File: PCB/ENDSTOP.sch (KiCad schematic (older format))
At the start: 4 parts, among them J9 ENDSTOP_CONN, SW3 ENDSTOP

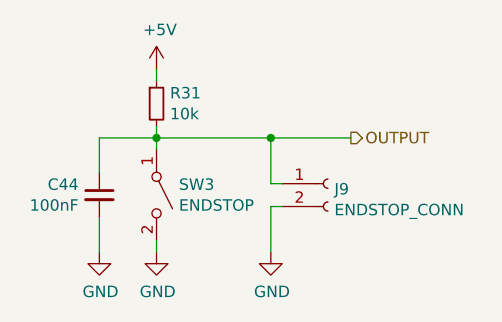
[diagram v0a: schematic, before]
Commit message: Added remaining test points
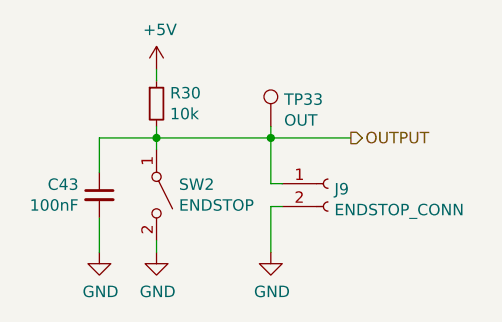
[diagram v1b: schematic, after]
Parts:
- added TP33: OUT, symbol Connector:TestPoint
- renumbered C44 to C43, R31 to R30, SW3 to SW2
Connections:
- net OUTPUT: now also TP33.1
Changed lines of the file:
@@
 OUTPUT
 $Comp
-L Switch:SW_SPST SW3
+L Switch:SW_SPST SW2
 U 1 1 5E8A8DC4
 P 6150 4150
-F 0 "SW3" V 6104 4248 50  0000 L CNN
+F 0 "SW2" V 6104 4248 50  0000 L CNN
 F 1 "ENDSTOP" V 6195 4248 50  0000 L CNN
 F 2 "" H 6150 4150 50  0001 C CNN
@@
 $EndComp
 $Comp
-L Device:C_Small C44
+L Device:C_Small C43
 U 1 1 5E8A9073
 P 5900 4150
-F 0 "C44" H 5809 4196 50  0000 R CNN
+F 0 "C43" H 5809 4196 50  0000 R CNN
 F 1 "100nF" H 5809 4105 50  0000 R CNN
 F 2 "" H 5900 4150 50  0001 C CNN
@@
 $EndComp
 $Comp
-L Device:R_Small R31
+L Device:R_Small R30
 U 1 1 5E8A974E
 P 6150 3750
-F 0 "R31" H 6209 3796 50  0000 L CNN
+F 0 "R30" H 6209 3796 50  0000 L CNN
 F 1 "10k" H 6209 3705 50  0000 L CNN
 F 2 "" H 6150 3750 50  0001 C CNN
@@
 	6150 3900 6150 3950
 $Comp
-L power:GND #PWR0125
+L power:GND #PWR0122
 U 1 1 5E8A9B1B
 P 5900 4400
-F 0 "#PWR0125" H 5900 4150 50  0001 C CNN
+F 0 "#PWR0122" H 5900 4150 50  0001 C CNN
 F 1 "GND" H 5905 4227 50  0000 C CNN
 F 2 "" H 5900 4400 50  0001 C CNN
@@
 $EndComp
 $Comp
-L power:GND #PWR0127
+L power:GND #PWR0124
 U 1 1 5E8A9B96
 P 6150 4400
-F 0 "#PWR0127" H 6150 4150 50  0001 C CNN
+F 0 "#PWR0124" H 6150 4150 50  0001 C CNN
 F 1 "GND" H 6155 4227 50  0000 C CNN
 F 2 "" H 6150 4400 50  0001 C CNN
@@
 	6650 3900 6150 3900
 $Comp
-L power:GND #PWR0128
+L power:GND #PWR0125
 U 1 1 5E8AD764
 P 6650 4400
-F 0 "#PWR0128" H 6650 4150 50  0001 C CNN
+F 0 "#PWR0125" H 6650 4150 50  0001 C CNN
 F 1 "GND" H 6655 4227 50  0000 C CNN
 F 2 "" H 6650 4400 50  0001 C CNN
@@
 P 6150 3600
 AR Path="/5E8A6686/5E90B50E" Ref="#PWR?"  Part="1"
-AR Path="/5E89F314/5E90B50E" Ref="#PWR0126"  Part="1"
-F 0 "#PWR0126" H 6150 3450 50  0001 C CNN
+AR Path="/5E89F314/5E90B50E" Ref="#PWR0123"  Part="1"
+F 0 "#PWR0123" H 6150 3450 50  0001 C CNN
 F 1 "+5V" H 6165 3773 50  0000 C CNN
 F 2 "" H 6150 3600 50  0001 C CNN
@@
 	1    0    0    -1
 $EndComp
+$Comp
+L Connector:TestPoint TP?
+U 1 1 5E9CF62E
+P 6650 3850
+AR Path="/5E9CF62E" Ref="TP?"  Part="1"
+AR Path="/5E89F314/5E9CF62E" Ref="TP33"  Part="1"
+F 0 "TP33" H 6708 3968 50  0000 L CNN
+F 1 "OUT" H 6708 3877 50  0000 L CNN
+F 2 "" H 6850 3850 50  0001 C CNN
+F 3 "~" H 6850 3850 50  0001 C CNN
+	1    6650 3850
+	1    0    0    -1
+$EndComp
+Wire Wire Line
+	6650 3850 6650 3900
 $EndSCHEMATC

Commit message: Added majority footprints
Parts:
- C43: footprint (none) -> Capacitor_SMD:C_0603_1608Metric
- J9: footprint (none) -> Connector_Molex:Molex_KK-254_AE-6410-02A_1x02_P2.54mm_Vertical
- R30: footprint (none) -> Resistor_SMD:R_0603_1608Metric
- TP33: footprint (none) -> custom:TestPoint_Pad_D1.5mm
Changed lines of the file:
@@
 F 0 "C43" H 5809 4196 50  0000 R CNN
 F 1 "100nF" H 5809 4105 50  0000 R CNN
-F 2 "" H 5900 4150 50  0001 C CNN
+F 2 "Capacitor_SMD:C_0603_1608Metric" H 5900 4150 50  0001 C CNN
 F 3 "" H 5900 4150 50  0001 C CNN
 F 4 "X7R" H 5900 4150 50  0001 C CNN "Dielectric"
@@
 F 0 "R30" H 6209 3796 50  0000 L CNN
 F 1 "10k" H 6209 3705 50  0000 L CNN
-F 2 "" H 6150 3750 50  0001 C CNN
+F 2 "Resistor_SMD:R_0603_1608Metric" H 6150 3750 50  0001 C CNN
 F 3 "" H 6150 3750 50  0001 C CNN
 	1    6150 3750
@@
 F 0 "J9" H 6928 4076 50  0000 L CNN
 F 1 "ENDSTOP_CONN" H 6928 3985 50  0000 L CNN
-F 2 "" H 6900 4100 50  0001 C CNN
+F 2 "Connector_Molex:Molex_KK-254_AE-6410-02A_1x02_P2.54mm_Vertical" H 6900 4100 50  0001 C CNN
 F 3 "" H 6900 4100 50  0001 C CNN
 	1    6900 4100
@@
 F 0 "TP33" H 6708 3968 50  0000 L CNN
 F 1 "OUT" H 6708 3877 50  0000 L CNN
-F 2 "" H 6850 3850 50  0001 C CNN
+F 2 "custom:TestPoint_Pad_D1.5mm" H 6850 3850 50  0001 C CNN
 F 3 "~" H 6850 3850 50  0001 C CNN
 	1    6650 3850
